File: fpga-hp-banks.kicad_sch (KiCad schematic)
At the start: 9 parts, among them U34 XCAU25P-2FFVB676I

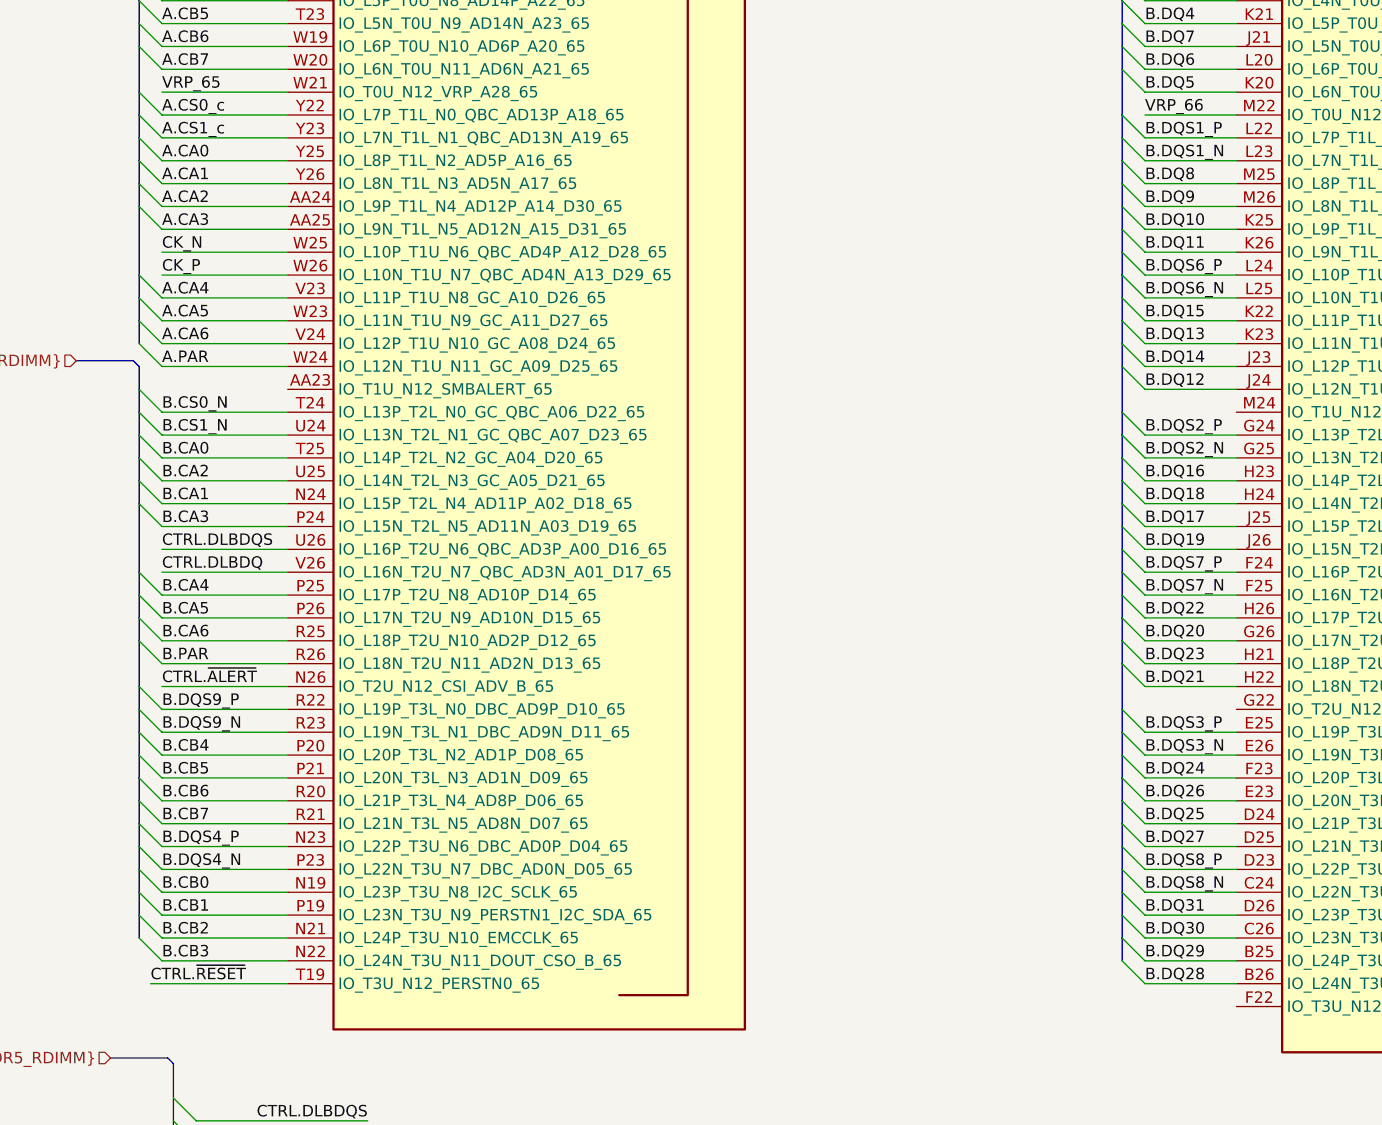
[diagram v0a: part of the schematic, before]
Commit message: [#66521] Add Layout for DDR5 B.CB[0..7]
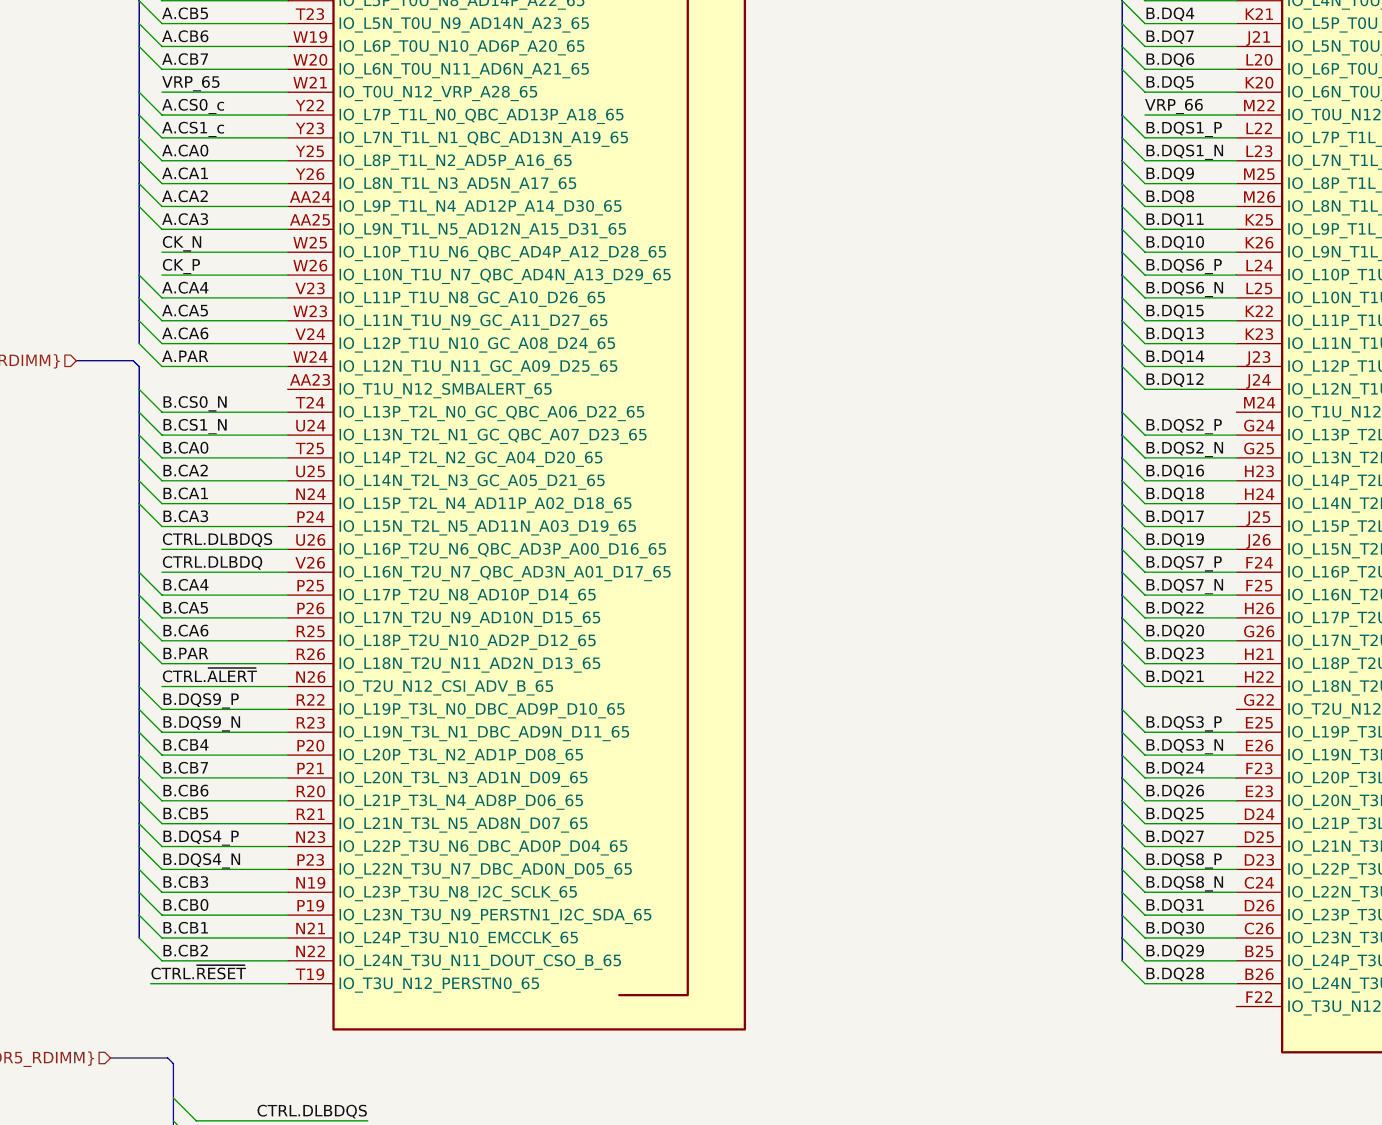
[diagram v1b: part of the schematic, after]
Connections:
- net B.CB0: now also U34.P19 (IO_L23N_T3U_N9_PERSTN1_I2C_SDA_65); no longer U34.N19 (IO_L23P_T3U_N8_I2C_SCLK_65)
- net B.CB1: now also U34.N21 (IO_L24P_T3U_N10_EMCCLK_65); no longer U34.P19 (IO_L23N_T3U_N9_PERSTN1_I2C_SDA_65)
- net B.CB2: now also U34.N22 (IO_L24N_T3U_N11_DOUT_CSO_B_65); no longer U34.N21 (IO_L24P_T3U_N10_EMCCLK_65)
- net B.CB3: now also U34.N19 (IO_L23P_T3U_N8_I2C_SCLK_65); no longer U34.N22 (IO_L24N_T3U_N11_DOUT_CSO_B_65)
- net B.CB5: now also U34.R21 (IO_L21N_T3L_N5_AD8N_D07_65); no longer U34.P21 (IO_L20N_T3L_N3_AD1N_D09_65)
- net B.CB7: now also U34.P21 (IO_L20N_T3L_N3_AD1N_D09_65); no longer U34.R21 (IO_L21N_T3L_N5_AD8N_D07_65)
- net B.DQ10: now also U34.K26 (IO_L9N_T1L_N5_AD12N_66); no longer U34.K25 (IO_L9P_T1L_N4_AD12P_66)
- net B.DQ11: now also U34.K25 (IO_L9P_T1L_N4_AD12P_66); no longer U34.K26 (IO_L9N_T1L_N5_AD12N_66)
- net B.DQ8: now also U34.M26 (IO_L8N_T1L_N3_AD5N_66); no longer U34.M25 (IO_L8P_T1L_N2_AD5P_66)
- net B.DQ9: now also U34.M25 (IO_L8P_T1L_N2_AD5P_66); no longer U34.M26 (IO_L8N_T1L_N3_AD5N_66)
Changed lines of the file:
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@@
     (effects (font (size 1.27 1.27)) (justify left bottom))
   )
-  (label "B.DQ8" (at 245.11 99.06 0) (fields_autoplaced)
+  (label "B.DQ8" (at 245.11 101.6 0) (fields_autoplaced)
     (effects (font (size 1.27 1.27)) (justify left bottom))
   )
@@
     (effects (font (size 1.27 1.27)) (justify left bottom))
   )
-  (label "B.CB0" (at 135.89 177.8 0) (fields_autoplaced)
+  (label "B.CB0" (at 135.89 180.34 0) (fields_autoplaced)
     (effects (font (size 1.27 1.27)) (justify left bottom))
   )
@@
     (effects (font (size 1.27 1.27)) (justify left bottom))
   )
-  (label "B.CB1" (at 135.89 180.34 0) (fields_autoplaced)
+  (label "B.CB1" (at 135.89 182.88 0) (fields_autoplaced)
     (effects (font (size 1.27 1.27)) (justify left bottom))
   )
@@
     (effects (font (size 1.27 1.27)) (justify left bottom))
   )
-  (label "B.DQ9" (at 245.11 101.6 0) (fields_autoplaced)
+  (label "B.DQ9" (at 245.11 99.06 0) (fields_autoplaced)
     (effects (font (size 1.27 1.27)) (justify left bottom))
   )
@@
     (effects (font (size 1.27 1.27)) (justify left bottom))
   )
-  (label "B.DQ10" (at 245.11 104.14 0) (fields_autoplaced)
+  (label "B.DQ10" (at 245.11 106.68 0) (fields_autoplaced)
     (effects (font (size 1.27 1.27)) (justify left bottom))
   )
@@
     (effects (font (size 1.27 1.27)) (justify left bottom))
   )
-  (label "B.CB2" (at 135.89 182.88 0) (fields_autoplaced)
-    (effects (font (size 1.27 1.27)) (justify left bottom))
-  )
-  (label "B.CB3" (at 135.89 185.42 0) (fields_autoplaced)
-    (effects (font (size 1.27 1.27)) (justify left bottom))
-  )
-  (label "B.CB7" (at 135.89 170.18 0) (fields_autoplaced)
+  (label "B.CB2" (at 135.89 185.42 0) (fields_autoplaced)
+    (effects (font (size 1.27 1.27)) (justify left bottom))
+  )
+  (label "B.CB3" (at 135.89 177.8 0) (fields_autoplaced)
+    (effects (font (size 1.27 1.27)) (justify left bottom))
+  )
+  (label "B.CB7" (at 135.89 165.1 0) (fields_autoplaced)
     (effects (font (size 1.27 1.27)) (justify left bottom))
   )
@@
     (effects (font (size 1.27 1.27)) (justify left bottom))
   )
-  (label "B.DQ11" (at 245.11 106.68 0) (fields_autoplaced)
+  (label "B.DQ11" (at 245.11 104.14 0) (fields_autoplaced)
     (effects (font (size 1.27 1.27)) (justify left bottom))
   )
@@
     (effects (font (size 1.27 1.27)) (justify left bottom))
   )
-  (label "B.CB5" (at 135.89 165.1 0) (fields_autoplaced)
-    (effects (font (size 1.27 1.27)) (justify left bottom))
-  )
+  (label "B.CB5" (at 135.89 170.18 0) (fields_autoplaced)
+    (effects (font (size 1.27 1.27)) (justify left bottom))
+  )

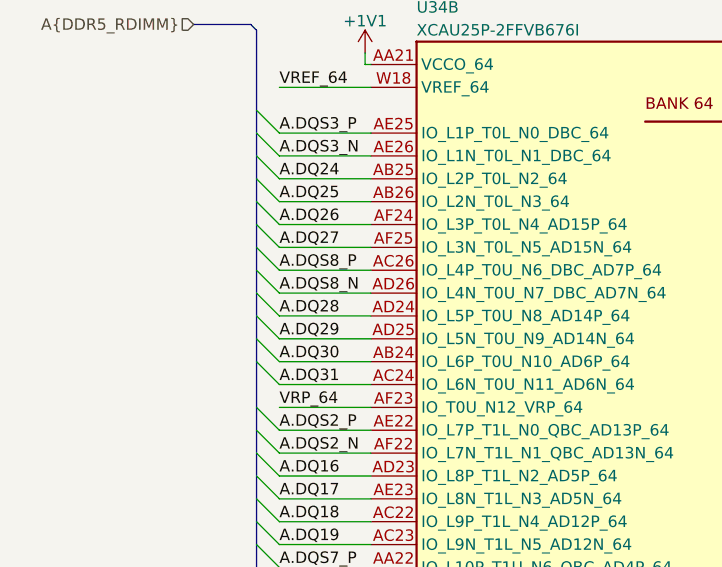
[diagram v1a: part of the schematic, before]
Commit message: [#66521] Add Layout for DDR5 A.DQ[23..31]
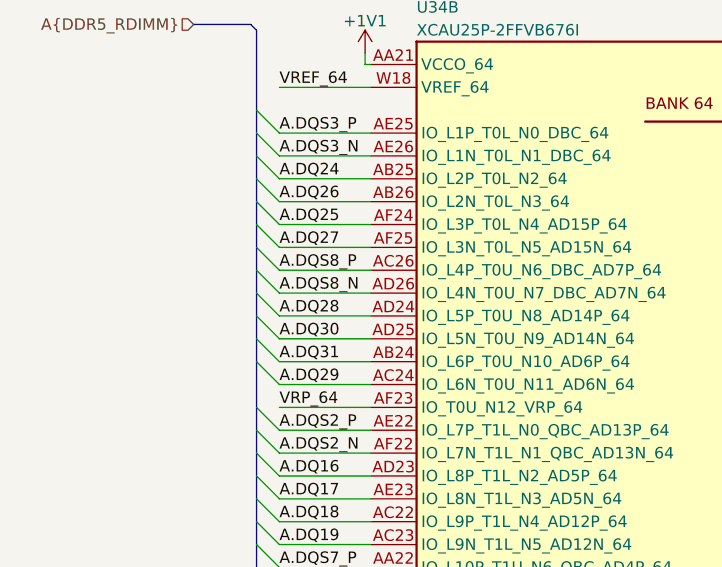
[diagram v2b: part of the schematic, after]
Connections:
- net A.DQ25: now also U34.AF24 (IO_L3P_T0L_N4_AD15P_64); no longer U34.AB26 (IO_L2N_T0L_N3_64)
- net A.DQ26: now also U34.AB26 (IO_L2N_T0L_N3_64); no longer U34.AF24 (IO_L3P_T0L_N4_AD15P_64)
- net A.DQ29: now also U34.AC24 (IO_L6N_T0U_N11_AD6N_64); no longer U34.AD25 (IO_L5N_T0U_N9_AD14N_64)
- net A.DQ30: now also U34.AD25 (IO_L5N_T0U_N9_AD14N_64); no longer U34.AB24 (IO_L6P_T0U_N10_AD6P_64)
- net A.DQ31: now also U34.AB24 (IO_L6P_T0U_N10_AD6P_64); no longer U34.AC24 (IO_L6N_T0U_N11_AD6N_64)
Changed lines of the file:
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@@
     (effects (font (size 1.27 1.27)) (justify left bottom))
   )
-  (label "A.DQ31" (at 38.1 86.36 0) (fields_autoplaced)
+  (label "A.DQ31" (at 38.1 83.82 0) (fields_autoplaced)
     (effects (font (size 1.27 1.27)) (justify left bottom))
   )
@@
     (effects (font (size 1.27 1.27)) (justify left bottom))
   )
-  (label "A.DQ29" (at 38.1 81.28 0) (fields_autoplaced)
+  (label "A.DQ29" (at 38.1 86.36 0) (fields_autoplaced)
     (effects (font (size 1.27 1.27)) (justify left bottom))
   )
@@
     (effects (font (size 1.27 1.27)) (justify left bottom))
   )
-  (label "A.DQ26" (at 38.1 68.58 0) (fields_autoplaced)
+  (label "A.DQ26" (at 38.1 66.04 0) (fields_autoplaced)
     (effects (font (size 1.27 1.27)) (justify left bottom))
   )
@@
     (effects (font (size 1.27 1.27)) (justify left bottom))
   )
-  (label "A.DQ30" (at 38.1 83.82 0) (fields_autoplaced)
+  (label "A.DQ30" (at 38.1 81.28 0) (fields_autoplaced)
     (effects (font (size 1.27 1.27)) (justify left bottom))
   )
@@
     (effects (font (size 1.27 1.27)) (justify left bottom))
   )
-  (label "A.DQ25" (at 38.1 66.04 0) (fields_autoplaced)
-    (effects (font (size 1.27 1.27)) (justify left bottom))
-  )
+  (label "A.DQ25" (at 38.1 68.58 0) (fields_autoplaced)
+    (effects (font (size 1.27 1.27)) (justify left bottom))
+  )
